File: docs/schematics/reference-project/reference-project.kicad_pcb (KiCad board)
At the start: 2 copper layers, 38 x 68 mm, 23 parts, among them J1 UART, Q1 MMBT3904, SW1 INPUT_0, SW2 INPUT_1, SW3 INPUT_2, SW4 INPUT_3, SW5 INPUT_4, SW6 INPUT_5, SW7 RESET, U1 74HC165D, U2 ATTINY85-20PU

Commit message: Updated to v2.
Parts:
- moved R5 22.1 mm to (50.5, 98.9), turned to 180 degrees
- moved R6 20.9 mm to (55.5, 98.9), turned to 0 degrees
- moved J1 17.9 mm to (75.5, 69.9)
- moved Q1 10.7 mm to (67.2, 75.0)
- moved D1 10.3 mm to (72.5, 75.2)
- moved BT1 9.20 mm to (61.5, 66.6)
- moved SW1 8.58 mm to (72.4, 112.8)
- moved SW3 8.57 mm to (63.8, 112.8)
- moved R7 7.99 mm to (59.6, 73.5), turned to 270 degrees
- moved R8 7.90 mm to (61.1, 81.7)
- moved LS1 7.85 mm to (67.6, 80.9)
- moved R9 7.67 mm to (68.7, 70.4)
- moved U2 5.67 mm to (62.2, 77.5)
- moved R2 4.15 mm to (67.3, 100.8), turned to 0 degrees
- moved R3 3.96 mm to (60.5, 100.8), turned to 180 degrees
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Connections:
- U2 pad 3: Net-(U1-Pad2) -> Net-(U1-Pad7)
- U2 pad 5: Net-(U1-Pad7) -> Net-(U1-Pad2)
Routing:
- net Net-(U1-Pad2): track 28.1 -> 8.72 mm, vias 2 -> 0
- net Net-(R3-Pad1): track 42.3 -> 29.1 mm
- net Net-(R2-Pad1): track 28.4 -> 15.5 mm
- net Net-(U1-Pad7): track 21.2 -> 31.7 mm
- net Net-(R6-Pad1): track 29.1 -> 19.0 mm
- net Net-(D1-Pad3): track 8.87 -> 17.5 mm
- net Net-(R4-Pad1): track 36.1 -> 29.6 mm
- net +3V3: track 176.4 -> 180.7 mm
- net Net-(U1-Pad1): track 6.75 -> 3.25 mm
- net Net-(J1-Pad2): track 6.28 -> 8.78 mm
- net Net-(D1-Pad1): track 19.2 -> 20.9 mm
- net Net-(R7-Pad2): track 69.9 -> 71.3 mm
- net Net-(LS1-Pad1): track 4.19 -> 5.55 mm
- net Net-(Q1-Pad1): track 6.96 -> 8.24 mm
- net Net-(R1-Pad1): track 32.3 -> 31.5 mm
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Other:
- board size 38 x 68 mm -> 37.7 x 63 mm

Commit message: Updated to v3.
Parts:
- removed D1: BAT54C, smd-semi:SOT-23
- removed J1: UART, footprints:Header_2_Pin
- removed Q1: MMBT3904, TO_SOT_Packages_SMD:SOT-23
- removed R4, R5, R6, R7, R9: 10K, Resistors_SMD:R_0805_HandSoldering
- removed R8: 220, Resistors_SMD:R_0805_HandSoldering
- removed SW3: INPUT_2, Buttons_Switches_SMD:SW_SPST_TL3342
- removed SW4: INPUT_3, Buttons_Switches_SMD:SW_SPST_TL3342
- removed SW5: INPUT_4, Buttons_Switches_SMD:SW_SPST_TL3342
- removed SW6: INPUT_5, Buttons_Switches_SMD:SW_SPST_TL3342
- removed SW7: RESET, Buttons_Switches_SMD:SW_SPST_TL3342
- removed U2: ATTINY85-20PU, Housings_DIP:DIP-8_W7.62mm
- BT1: footprint Connectors:bornier2 -> reference-project-footprints:bornier2
- LS1: footprint Buzzers_Beepers:Buzzer_12x9.5RM7.6 -> reference-project-footprints:Buzzer_12x9.5RM7.6; moved to B.Cu
- R1, R2: footprint Resistors_SMD:R_0805_HandSoldering -> Resistors_SMD:R_0805
- R3: value 10K -> 220; footprint Resistors_SMD:R_0805_HandSoldering -> Resistors_SMD:R_0805
- SW1: value INPUT_0 -> RESET
- SW2: value INPUT_1 -> INPUT_5
- U1: value 74HC165D -> ATTINY85-20PU; footprint footprints:SOIC_16_0.154IN -> reference-project-footprints:DIP-8_W7.62mm; moved to B.Cu
- moved BT1 50.2 mm to (65.7, 116.7)
- moved LS1 25.7 mm to (65.3, 106.5)
- moved U1 15.1 mm to (61.6, 106.5), turned to 90 degrees
- moved SW1 13.9 mm to (58.6, 111.2), turned to 180 degrees
- moved R1 13.6 mm to (54.2, 102.7)
- moved SW2 6.27 mm to (67.7, 111.2), turned to 0 degrees
- moved R2 5.95 mm to (69.1, 106.5)
- moved R3 1.97 mm to (61.1, 102.7)
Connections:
- R1 pad 1: Net-(R1-Pad1) -> +3V3
- R1 pad 2: GND -> Net-(R1-Pad2)
- R3 pad 1: Net-(R3-Pad1) -> Net-(LS1-Pad1)
- R3 pad 2: GND -> Net-(R3-Pad2)
- SW1 pad 1: +3V3 -> GND
- SW1 pad 2: Net-(R1-Pad1) -> Net-(R1-Pad2)
- SW2 pad 1: +3V3 -> Net-(R2-Pad1)
- SW2 pad 2: Net-(R2-Pad1) -> +3V3
- U1 pad 1: Net-(U1-Pad1) -> (no net)
- U1 pad 2: Net-(U1-Pad2) -> Net-(R1-Pad2)
- U1 pad 3: Net-(R5-Pad1) -> Net-(R2-Pad1)
- U1 pad 4: Net-(R6-Pad1) -> GND
- U1 pad 5: GND -> (no net)
- U1 pad 6: GND -> Net-(R3-Pad2)
- U1 pad 7: Net-(U1-Pad7) -> (no net)
- U1 pad 8: GND -> +3V3
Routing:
- net +3V3: track 180.7 -> 64.0 mm
- net Net-(R7-Pad2): track 71.3 -> 0.00 mm
- net Net-(R5-Pad1): track 39.4 -> 0.00 mm
- net GND: track 0.00 -> 38.3 mm
- net Net-(U1-Pad7): track 31.7 -> 0.00 mm, vias 2 -> 0
- net Net-(R1-Pad1): track 31.5 -> 0.00 mm
- net Net-(R4-Pad1): track 29.6 -> 0.00 mm
- net Net-(R3-Pad1): track 29.1 -> 0.00 mm
- net Net-(D1-Pad1): track 20.9 -> 0.00 mm
- net Net-(R6-Pad1): track 19.0 -> 0.00 mm
- net Net-(D1-Pad3): track 17.5 -> 0.00 mm
- net Net-(R1-Pad2): track 0.00 -> 10.9 mm
- net Net-(J1-Pad2): track 8.78 -> 0.00 mm
- net Net-(U1-Pad2): track 8.72 -> 0.00 mm
- net Net-(Q1-Pad1): track 8.24 -> 0.00 mm
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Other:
- board size 37.7 x 63 mm -> 26.3 x 26.5 mm
- net class Default: clearance 0.3 -> 0.4
- rule trace_clearance: 0.3 -> 0.4

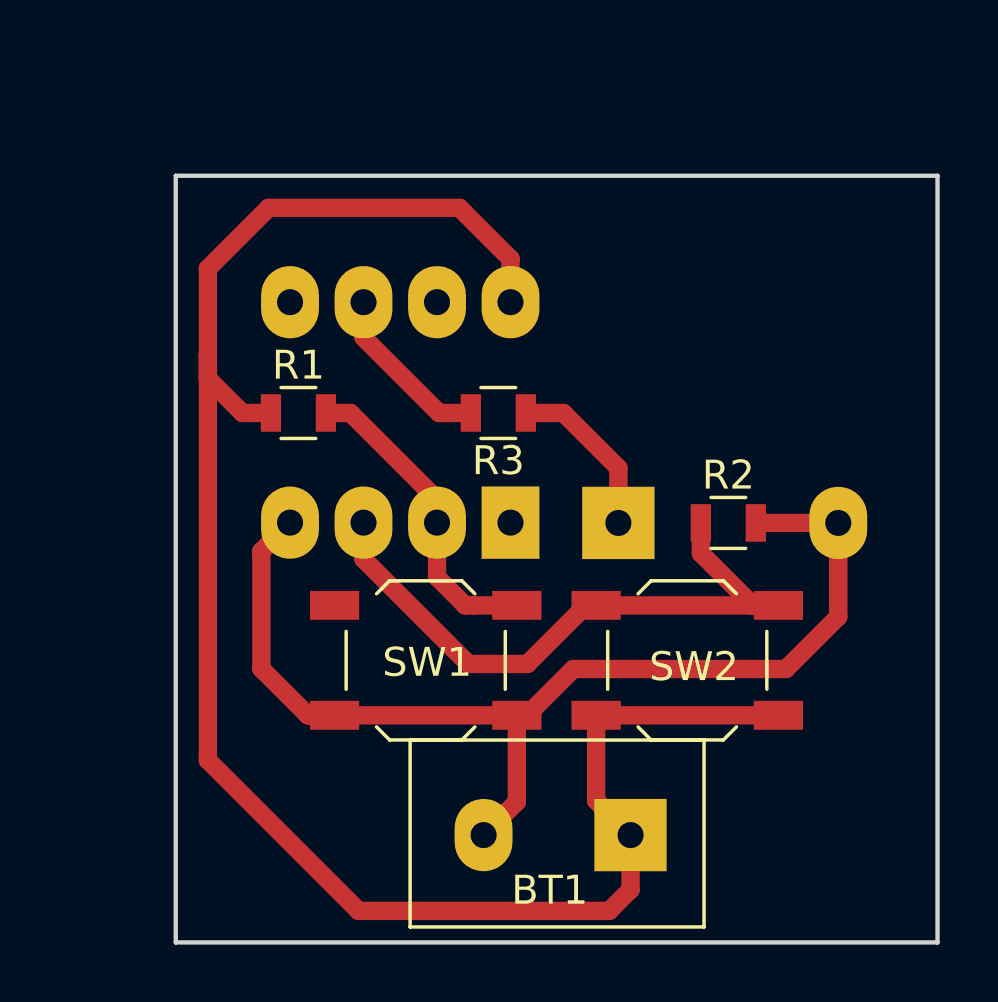
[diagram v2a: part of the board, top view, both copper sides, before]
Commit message: Full SMD version.
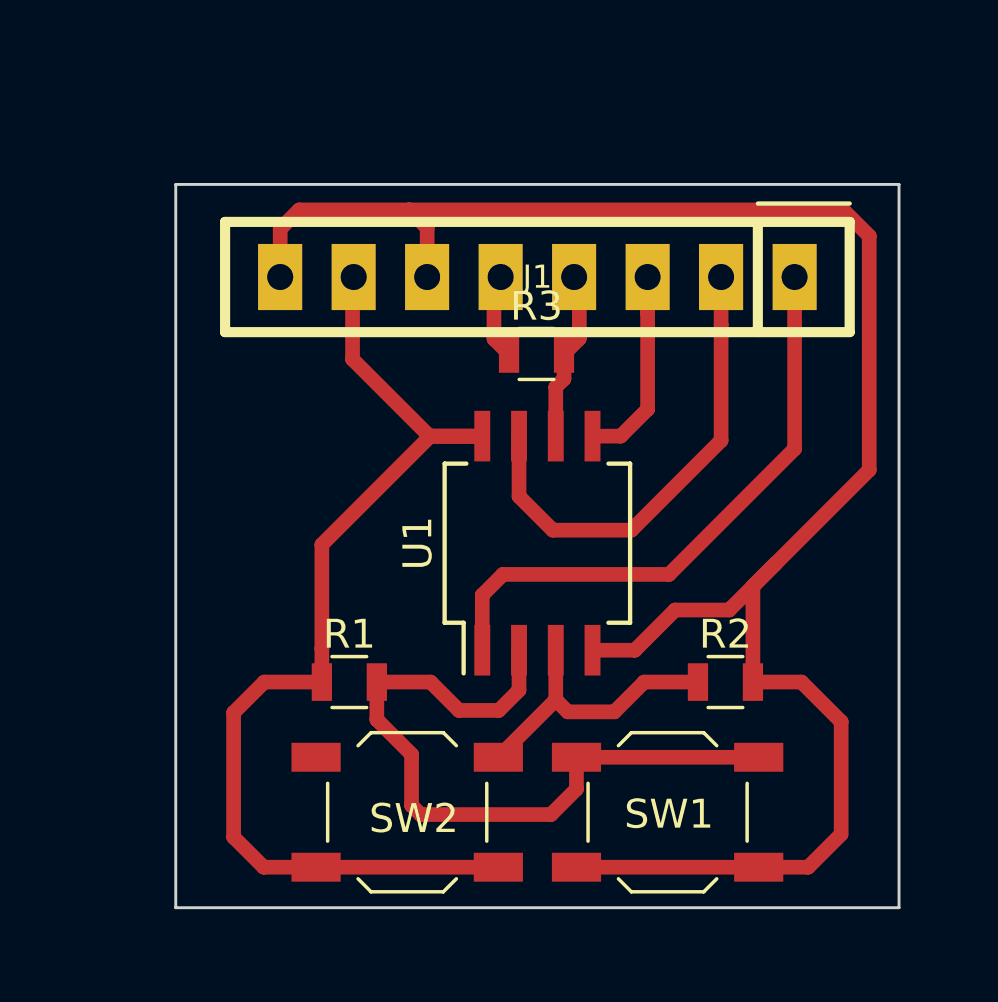
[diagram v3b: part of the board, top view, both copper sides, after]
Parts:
- removed BT1: CELL, reference-project-footprints:bornier2
- removed LS1: Buzzer, reference-project-footprints:Buzzer_12x9.5RM7.6
- added J1: Conn_01x08_Female, conn-100mil:CONN-100MIL-F-1x8, F.Cu at (62.5, 98.0)
- U1: value ATTINY85-20PU -> ATTINY85-20SU; footprint reference-project-footprints:DIP-8_W7.62mm -> Housings_SOIC:SO-8_5.3x6.2mm_Pitch1.27mm; moved to F.Cu
- moved SW2 11.0 mm to (58.0, 116.5)
- moved SW1 9.87 mm to (67.0, 116.5)
- moved R1 9.47 mm to (56.0, 112.0)
- moved R2 5.50 mm to (69.0, 112.0)
- moved R3 2.43 mm to (62.5, 100.7), turned to 0 degrees
- moved U1 1.17 mm to (62.5, 107.2)
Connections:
- net +3V3 renamed VCC
- net Net-(R3-Pad2) renamed PIN_6
- R3 pad 1: Net-(LS1-Pad1) -> SPKR+
- U1 pad 1: (no net) -> PIN_1
- U1 pad 5: (no net) -> PIN_5
- U1 pad 7: (no net) -> PIN_7
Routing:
- net GND: track 38.3 -> 67.0 mm
- net VCC: track 64.0 -> 37.2 mm
- net PIN_1: track 0.00 -> 20.7 mm
- net PIN_7: track 0.00 -> 16.5 mm
- net Net-(R1-Pad2): track 10.9 -> 25.3 mm
- net Net-(R2-Pad1): track 22.4 -> 10.0 mm
- net PIN_5: track 0.00 -> 6.86 mm
- net Net-(LS1-Pad1): track 5.81 -> 0.00 mm
- net SPKR+: track 0.00 -> 3.07 mm
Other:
- board size 26.3 x 26.5 mm -> 25 x 25 mm

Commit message: Update KiCad schematics. Upgrade Platformio to 3.5.x.
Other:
- net class Default: clearance 0.4 -> 0.6
- rule trace_clearance: 0.4 -> 0.6
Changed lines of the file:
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@@
   )
   (setup
-    (last_trace_width 0.508)
+    (last_trace_width 0.254)
     (user_trace_width 0.254)
     (user_trace_width 0.381)
@@
     (user_trace_width 0.762)
     (user_trace_width 0.8128)
-    (trace_clearance 0.4)
+    (trace_clearance 0.6)
     (zone_clearance 0.35)
     (zone_45_only yes)
@@
     (mod_text_size 1 1)
     (mod_text_width 0.15)
-    (pad_size 1.524 2.286)
+    (pad_size 1.7 1)
     (pad_drill 0.9)
     (pad_to_mask_clearance 0.2)
@@
     (visible_elements FFFFFF99)
     (pcbplotparams
-      (layerselection 0x01000_7ffffffe)
+      (layerselection 0x00000_7fffffff)
       (usegerberextensions false)
       (usegerberattributes true)
@@
       (padsonsilk true)
       (subtractmaskfromsilk false)
-      (outputformat 1)
+      (outputformat 3)
       (mirror false)
-      (drillshape 0)
+      (drillshape 2)
       (scaleselection 1)
       (outputdirectory gerbers/))
@@
   (net 9 VCC)
   (net_class Default "This is the default net class."
-    (clearance 0.4)
+    (clearance 0.6)
     (trace_width 0.381)
     (via_dia 1.5)
@@
     (pad 8 thru_hole trapezoid (at 8.89 0 180) (size 1.524 2.286) (drill 0.9) (layers *.Cu *.Mask F.SilkS)
       (net 1 GND))
-    (model pin_strip/pin_socket_8.wrl
-      (at (xyz 0 0 0))
-      (scale (xyz 1 1 1))
-      (rotate (xyz 0 0 0))
-    )
-  )
+    (model "${KIPRJMOD}/3d models/Socket_Female_1x8.step"
+      (at (xyz 0.2992125984251969 -0.05118110236220473 -0.06299212598425198))
+      (scale (xyz 1 1 1))
+      (rotate (xyz 90 0 90))
+    )
+  )
